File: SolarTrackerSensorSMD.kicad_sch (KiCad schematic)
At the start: 49 parts, among them J1 Conn_01x03_Male, J2 Conn_01x03_Male, J3 Conn_01x03_Male, J4 Conn_01x03_Male, J5 Conn_01x07_Male, J6 Conn_01x05_Male, U1 LM339, U2 7404, U3 7408, U4 7408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

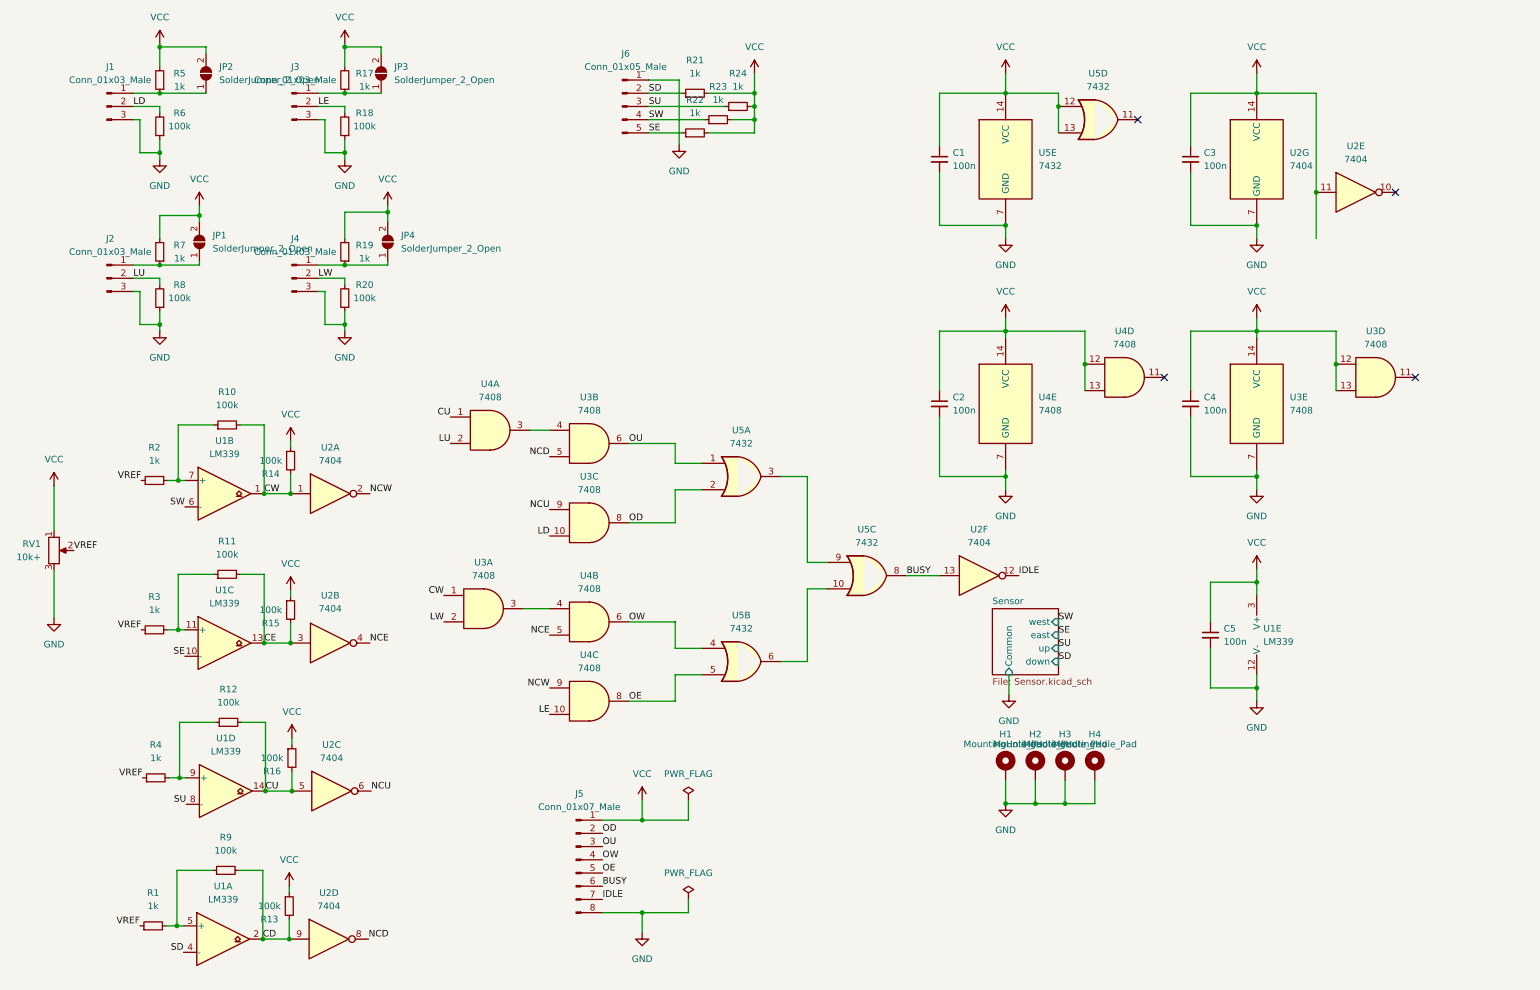
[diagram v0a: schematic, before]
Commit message: Replace Idle with Busy_UD & Busy_EW
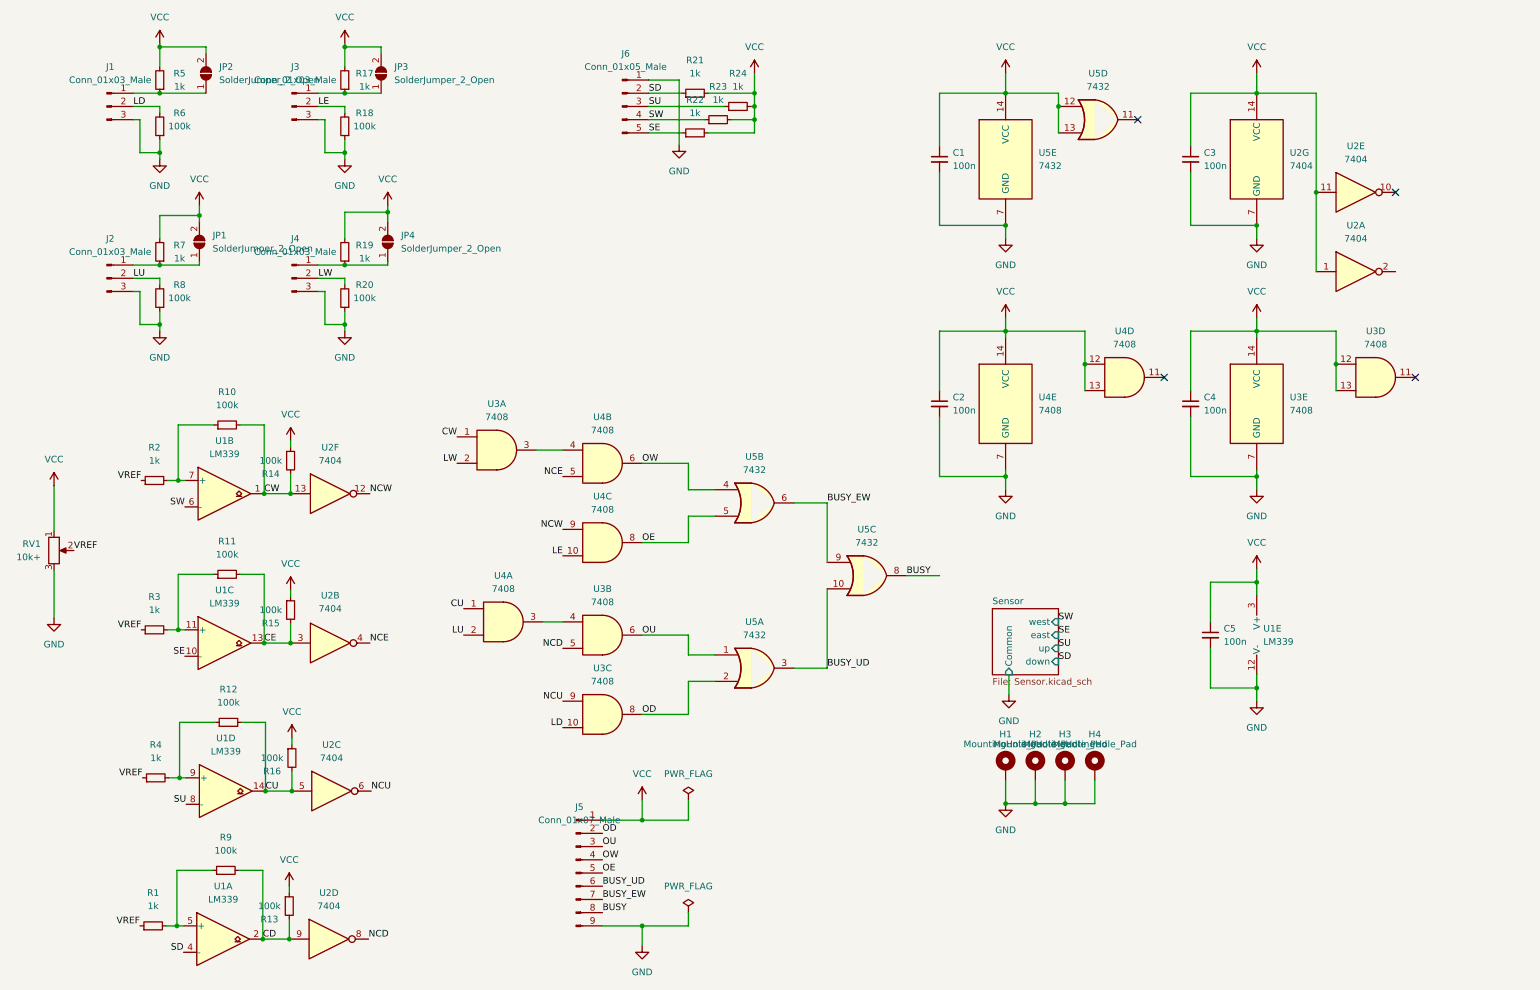
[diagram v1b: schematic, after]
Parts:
- J5: footprint Connector_PinHeader_2.54mm:PinHeader_1x08_P2.54mm_Vertical -> Connector_PinHeader_2.54mm:PinHeader_1x09_P2.54mm_Vertical; symbol Connector:Conn_01x08_Male -> Connector:Conn_01x09_Male
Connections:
- net BUSY: now also J5.8 (Pin_8); no longer J5.6 (Pin_6), U2.13
- net CW: now also U2.13; no longer U2.1
- net GND: now also J5.9 (Pin_9); no longer J5.8 (Pin_8)
- net NCW: now also U2.12; no longer U2.2
- net VCC: now also U2.1
- net BUSY_EW: now reaches U5.6
- net BUSY_EW: now also J5.7 (Pin_7), U5.9; no longer U5.10
- net BUSY_UD: now reaches U5.3
- net BUSY_UD: now also J5.6 (Pin_6), U5.10; no longer U5.9
- removed net IDLE: J5.7 (Pin_7), U2.12
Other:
- moved on the sheet: U2A, U3A, U3B, U3C, U4A, U4B, U4C, U5A, U5B

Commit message: Add licence & reshuffle silkscreen graphics
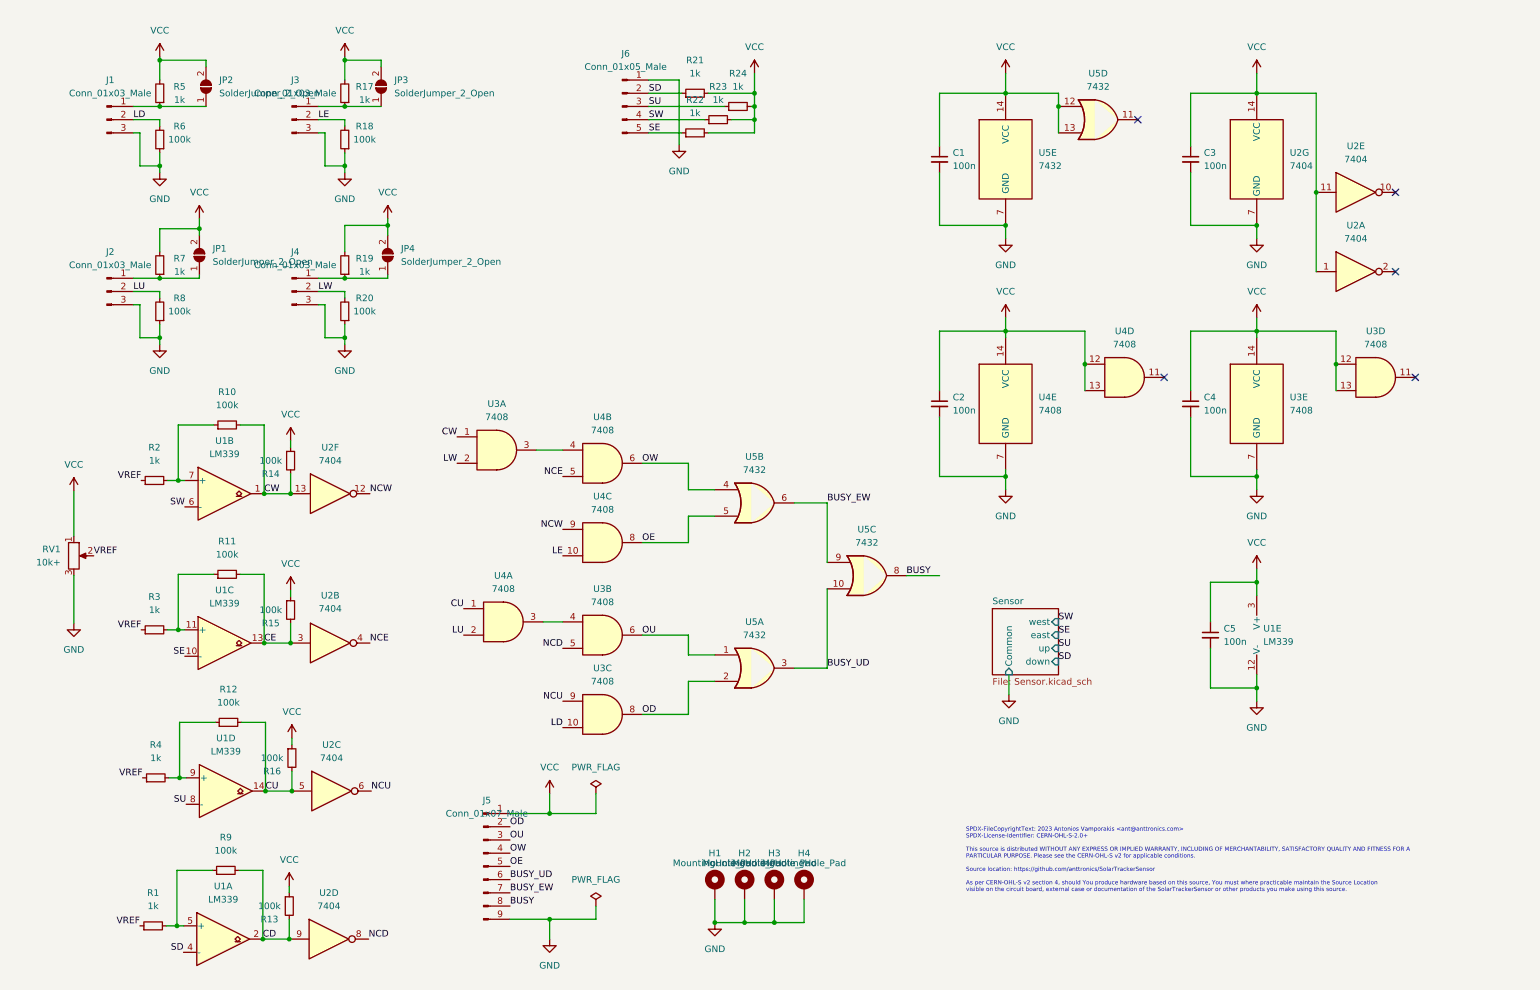
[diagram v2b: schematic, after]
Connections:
- no-connect marks 4 -> 5
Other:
- note added: "SPDX-FileCopyrightText: 2023 Antonios Vamporakis <ant@anttronics.com> SPDX-License-Identifier: CERN-OHL-S-2.0+ This source is distributed WITHOUT ANY EXPRESS OR IMPLIED WARRANTY, INCLUDING OF MERCHANTABILITY, SATISFACTORY QUALITY AND FITNESS FOR A PARTICULAR PURPOSE. Please see the CERN-OHL-S v2 for applicable conditions. Source location: https://github.com/anttronics/SolarTrackerSensor As per CE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"
- company: (none) -> AntTronics
- title: (none) -> SolarTrackerSensor
- moved on the sheet: H1, H2, H3, H4, J1, J2, J3, J4, J5, JP1, JP2, JP3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

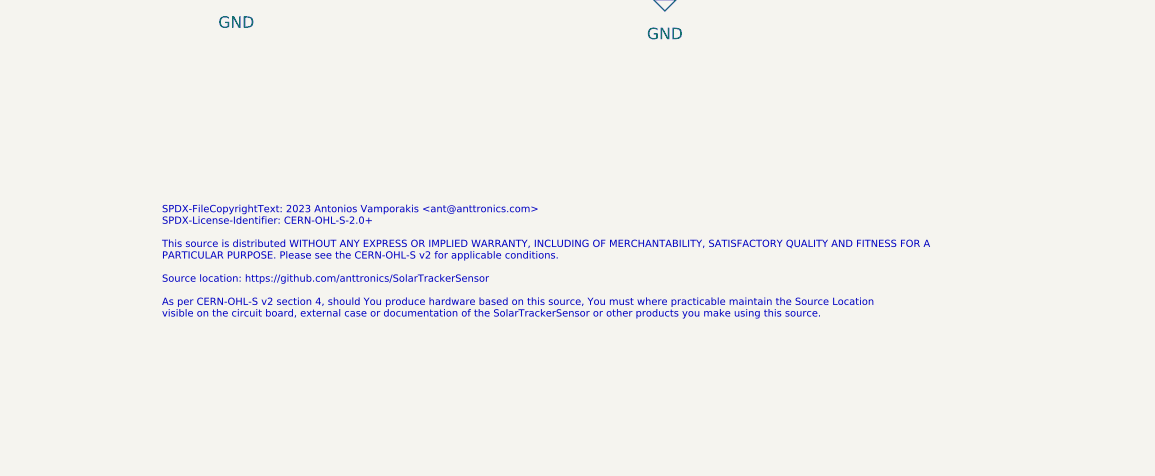
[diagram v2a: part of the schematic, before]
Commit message: CERN OHL W seems more appropriate
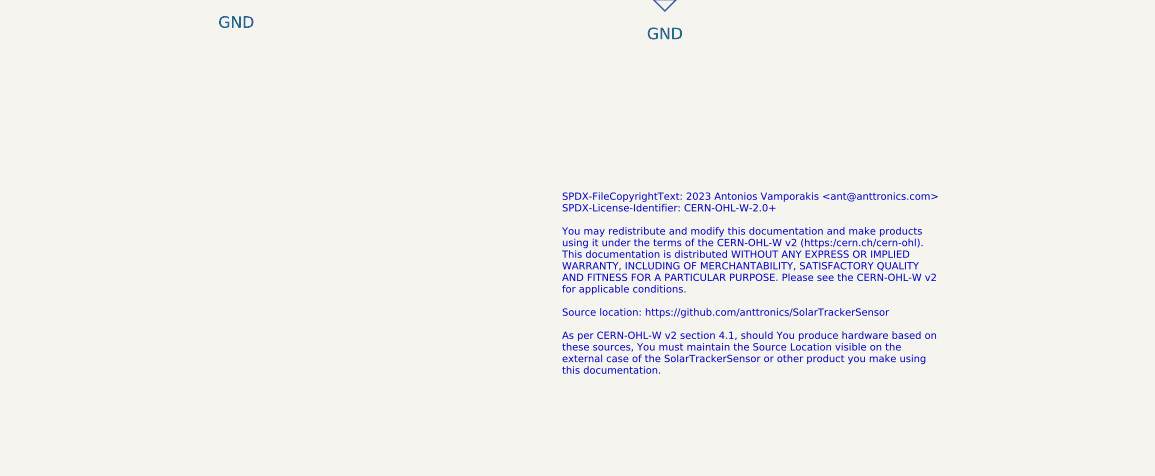
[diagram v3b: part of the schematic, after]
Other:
- note added: "SPDX-FileCopyrightText: 2023 Antonios Vamporakis <ant@anttronics.com> SPDX-License-Identifier: CERN-OHL-W-2.0+ You may redistribute and modify this documentation and make products using it under the terms of the CERN-OHL-W v2 (https:/cern.ch/cern-ohl). This documentation is distributed WITHOUT ANY EXPRESS OR IMPLIED WARRANTY, INCLUDING OF MERCHANTABILITY, SATISFACTORY QUALITY AND FITNESS FOR A PA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"
- note removed: "SPDX-FileCopyrightText: 2023 Antonios Vamporakis <ant@anttronics.com> SPDX-License-Identifier: CERN-OHL-S-2.0+ This source is distributed WITHOUT ANY EXPRESS OR IMPLIED WARRANTY, INCLUDING OF MERCHANTABILITY, SATISFACTORY QUALITY AND FITNESS FOR A PARTICULAR PURPOSE. Please see the CERN-OHL-S v2 for applicable conditions. Source location: https://github.com/anttronics/SolarTrackerSensor As per CE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"
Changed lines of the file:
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@@
     (stroke (width 0) (type default) (color 0 0 0 0))
   )
-  (text "SPDX-FileCopyrightText: 2023 Antonios Vamporakis <ant@anttronics.com>\nSPDX-License-Identifier: CERN-OHL-S-2.0+\n\nThis source is distributed WITHOUT ANY EXPRESS OR IMPLIED WARRANTY, INCLUDING OF MERCHANTABILITY, SATISFACTORY QUALITY AND FITNESS FOR A \nPARTICULAR PURPOSE. Please see the CERN-OHL-S v2 for applicable conditions.\n\nSource location: https://github.com/anttronics/SolarTrackerSensor\n\nAs per CERN-OHL-S v2 section 4, should You produce hardware based on this source, You must where practicable maintain the Source Location \nvisible on the circuit board, external case or documentation of the SolarTrackerSensor or other products you make using this source.\n"
-    (at 191.77 180.34 0)
+  (text "SPDX-FileCopyrightText: 2023 Antonios Vamporakis <ant@anttronics.com>\nSPDX-License-Identifier: CERN-OHL-W-2.0+\n\nYou may redistribute and modify this documentation and make products\nusing it under the terms of the CERN-OHL-W v2 (https:/cern.ch/cern-ohl).\nThis documentation is distributed WITHOUT ANY EXPRESS OR IMPLIED\nWARRANTY, INCLUDING OF MERCHANTABILITY, SATISFACTORY QUALITY\nAND FITNESS FOR A PARTICULAR PURPOSE. Please see the CERN-OHL-W v2\nfor applicable conditions.\n\nSource location: https://github.com/anttronics/SolarTrackerSensor\n\nAs per CERN-OHL-W v2 section 4.1, should You produce hardware based on\nthese sources, You must maintain the Source Location visible on the\nexternal case of the SolarTrackerSensor or other product you make using\nthis documentation.\n"
+    (at 236.22 186.69 0)
     (effects (font (size 0.8 0.8)) (justify left bottom))
   )
